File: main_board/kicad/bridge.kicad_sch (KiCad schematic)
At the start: 21 parts, among them Q1 IRFB3077, Q2 IRFB3077, Q3 IRFB3077, Q4 IRFB3077, Q5 IRFB3077, Q6 IRFB3077

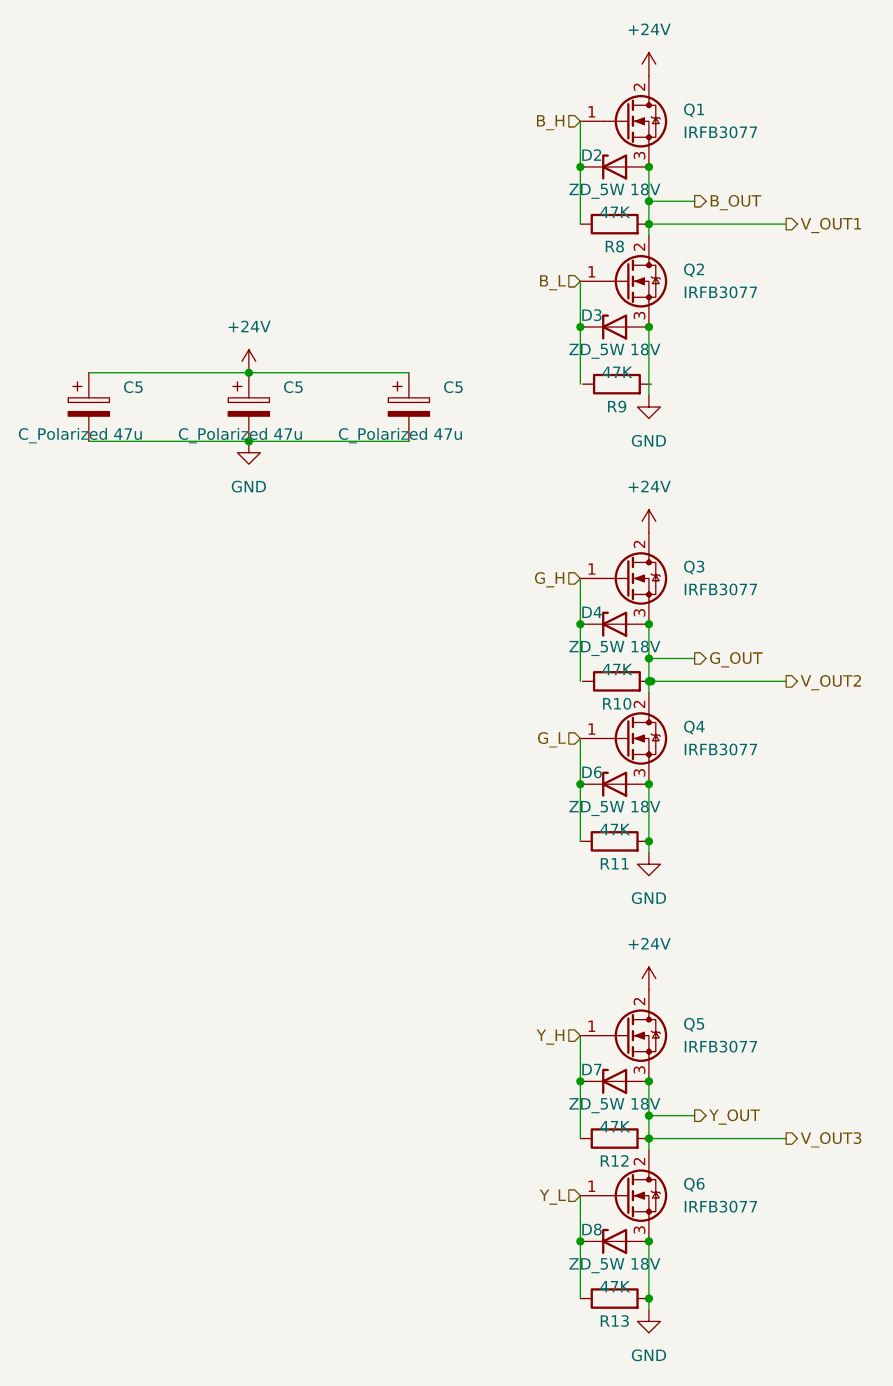
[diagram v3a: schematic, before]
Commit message: added LEDS and fuses
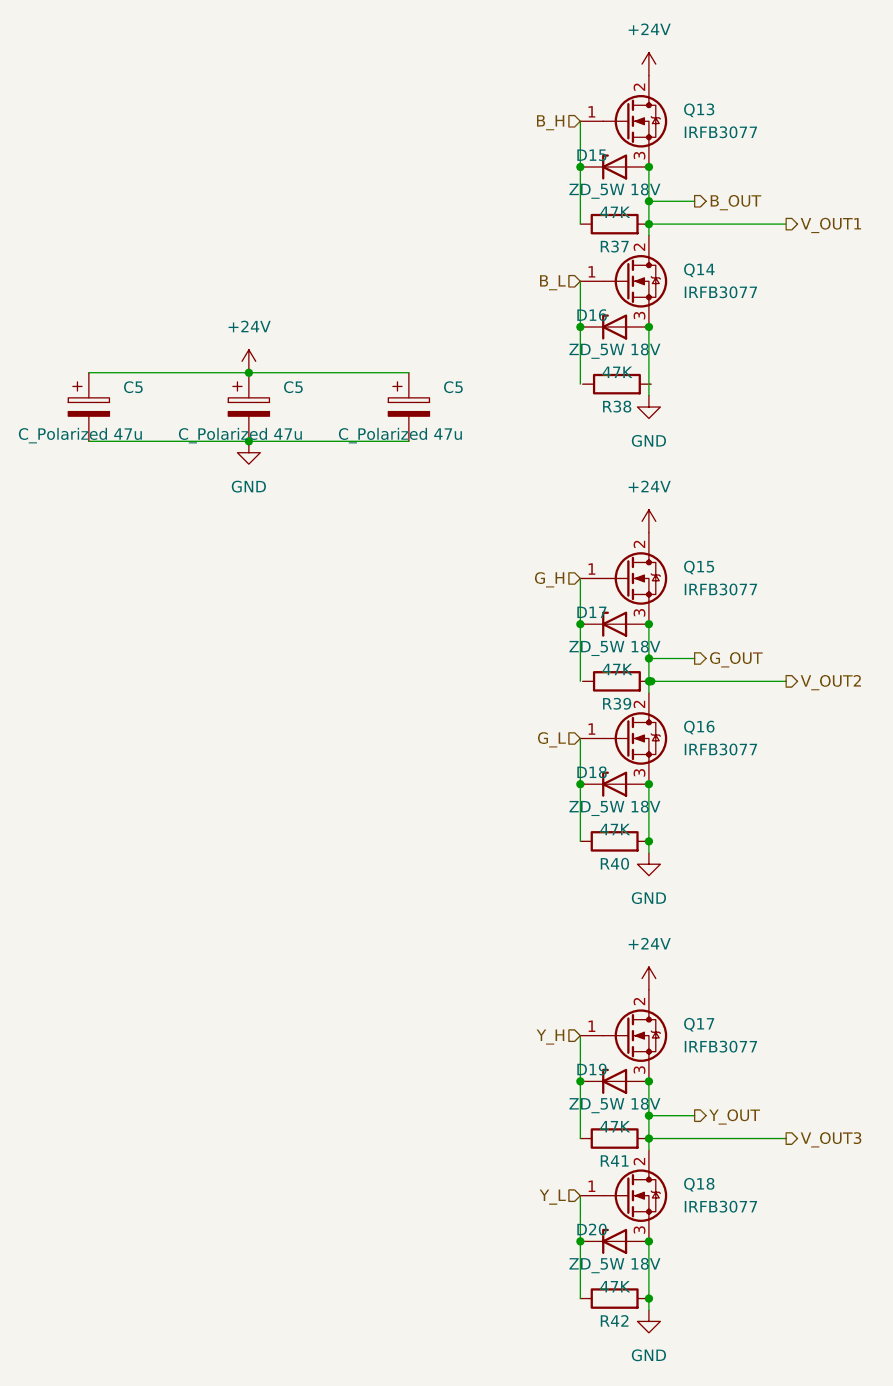
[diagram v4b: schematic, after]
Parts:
- renumbered D2 to D15, D3 to D16, D4 to D17, D6 to D18, D7 to D19, D8 to D20, Q1 to Q13, Q2 to Q14, Q3 to Q15, Q4 to Q16, Q5 to Q17, Q6 to Q18, R8 to R37, R9 to R38, R10 to R39, R11 to R40, R12 to R41, R13 to R42
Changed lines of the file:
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@@
   (symbol (lib_id "2022-lsd:IRFB3077") (at 114.3 137.16 0) (unit 1)
     (in_bom yes) (on_board yes) (dnp no) (fields_autoplaced)
-    (property "Reference" "Q5" (at 120.65 135.89 0)
+    (property "Reference" "Q17" (at 120.65 135.89 0)
       (effects (font (size 1.27 1.27)) (justify left))
     )
@@
   (symbol (lib_id "Device:R") (at 113.03 115.57 90) (unit 1)
     (in_bom yes) (on_board yes) (dnp no)
-    (property "Reference" "R11" (at 113.03 118.11 90)
+    (property "Reference" "R40" (at 113.03 118.11 90)
       (effects (font (size 1.27 1.27)))
     )
@@
   (symbol (lib_id "2022-lsd:IRFB3077") (at 114.3 86.36 0) (unit 1)
     (in_bom yes) (on_board yes) (dnp no)
-    (property "Reference" "Q3" (at 120.65 85.09 0)
+    (property "Reference" "Q15" (at 120.65 85.09 0)
       (effects (font (size 1.27 1.27)) (justify left))
     )
@@
   (symbol (lib_id "power:+24V") (at 116.84 81.28 0) (unit 1)
     (in_bom yes) (on_board yes) (dnp no) (fields_autoplaced)
-    (property "Reference" "#PWR026" (at 116.84 85.09 0)
+    (property "Reference" "#PWR069" (at 116.84 85.09 0)
       (effects (font (size 1.27 1.27)) hide)
     )
@@
   (symbol (lib_id "power:+24V") (at 72.39 63.5 0) (unit 1)
     (in_bom yes) (on_board yes) (dnp no) (fields_autoplaced)
-    (property "Reference" "#PWR021" (at 72.39 67.31 0)
+    (property "Reference" "#PWR065" (at 72.39 67.31 0)
       (effects (font (size 1.27 1.27)) hide)
     )
@@
   (symbol (lib_id "Diode:1N53xxB") (at 113.03 160.02 0) (unit 1)
     (in_bom yes) (on_board yes) (dnp no)
-    (property "Reference" "D8" (at 110.49 158.75 0)
+    (property "Reference" "D20" (at 110.49 158.75 0)
       (effects (font (size 1.27 1.27)))
     )
@@
   (symbol (lib_id "Device:R") (at 113.284 97.79 90) (unit 1)
     (in_bom yes) (on_board yes) (dnp no)
-    (property "Reference" "R10" (at 113.284 100.33 90)
+    (property "Reference" "R39" (at 113.284 100.33 90)
       (effects (font (size 1.27 1.27)))
     )
@@
   (symbol (lib_id "Diode:1N53xxB") (at 113.03 109.22 0) (unit 1)
     (in_bom yes) (on_board yes) (dnp no)
-    (property "Reference" "D6" (at 110.49 107.95 0)
+    (property "Reference" "D18" (at 110.49 107.95 0)
       (effects (font (size 1.27 1.27)))
     )
@@
   (symbol (lib_id "2022-lsd:IRFB3077") (at 114.3 154.94 0) (unit 1)
     (in_bom yes) (on_board yes) (dnp no) (fields_autoplaced)
-    (property "Reference" "Q6" (at 120.65 153.67 0)
+    (property "Reference" "Q18" (at 120.65 153.67 0)
       (effects (font (size 1.27 1.27)) (justify left))
     )
@@
   (symbol (lib_id "Diode:1N53xxB") (at 113.03 142.24 0) (unit 1)
     (in_bom yes) (on_board yes) (dnp no)
-    (property "Reference" "D7" (at 110.49 140.97 0)
+    (property "Reference" "D19" (at 110.49 140.97 0)
       (effects (font (size 1.27 1.27)))
     )
@@
   (symbol (lib_id "Device:R") (at 113.284 64.77 90) (unit 1)
     (in_bom yes) (on_board yes) (dnp no)
-    (property "Reference" "R9" (at 113.284 67.31 90)
+    (property "Reference" "R38" (at 113.284 67.31 90)
       (effects (font (size 1.27 1.27)))
     )
@@
   (symbol (lib_id "power:GND") (at 116.84 66.04 0) (unit 1)
     (in_bom yes) (on_board yes) (dnp no) (fields_autoplaced)
-    (property "Reference" "#PWR025" (at 116.84 72.39 0)
+    (property "Reference" "#PWR068" (at 116.84 72.39 0)
       (effects (font (size 1.27 1.27)) hide)
     )
@@
   (symbol (lib_id "power:+24V") (at 116.84 30.48 0) (unit 1)
     (in_bom yes) (on_board yes) (dnp no) (fields_autoplaced)
-    (property "Reference" "#PWR024" (at 116.84 34.29 0)
+    (property "Reference" "#PWR067" (at 116.84 34.29 0)
       (effects (font (size 1.27 1.27)) hide)
     )
@@
   (symbol (lib_id "Device:R") (at 113.03 46.99 90) (unit 1)
     (in_bom yes) (on_board yes) (dnp no)
-    (property "Reference" "R8" (at 113.03 49.53 90)
+    (property "Reference" "R37" (at 113.03 49.53 90)
       (effects (font (size 1.27 1.27)))
     )
@@
   (symbol (lib_id "power:GND") (at 72.39 71.12 0) (unit 1)
     (in_bom yes) (on_board yes) (dnp no) (fields_autoplaced)
-    (property "Reference" "#PWR023" (at 72.39 77.47 0)
+    (property "Reference" "#PWR066" (at 72.39 77.47 0)
       (effects (font (size 1.27 1.27)) hide)
     )
@@
   (symbol (lib_id "2022-lsd:IRFB3077") (at 114.3 53.34 0) (unit 1)
     (in_bom yes) (on_board yes) (dnp no) (fields_autoplaced)
-    (property "Reference" "Q2" (at 120.65 52.07 0)
+    (property "Reference" "Q14" (at 120.65 52.07 0)
       (effects (font (size 1.27 1.27)) (justify left))
     )
@@
   (symbol (lib_id "Diode:1N53xxB") (at 113.03 40.64 0) (unit 1)
     (in_bom yes) (on_board yes) (dnp no)
-    (property "Reference" "D2" (at 110.49 39.37 0)
+    (property "Reference" "D15" (at 110.49 39.37 0)
       (effects (font (size 1.27 1.27)))
     )
@@
   (symbol (lib_id "power:GND") (at 116.84 116.84 0) (unit 1)
     (in_bom yes) (on_board yes) (dnp no) (fields_autoplaced)
-    (property "Reference" "#PWR027" (at 116.84 123.19 0)
+    (property "Reference" "#PWR070" (at 116.84 123.19 0)
       (effects (font (size 1.27 1.27)) hide)
     )
@@
   (symbol (lib_id "power:+24V") (at 116.84 132.08 0) (unit 1)
     (in_bom yes) (on_board yes) (dnp no) (fields_autoplaced)
-    (property "Reference" "#PWR028" (at 116.84 135.89 0)
+    (property "Reference" "#PWR071" (at 116.84 135.89 0)
       (effects (font (size 1.27 1.27)) hide)
     )
@@
   (symbol (lib_id "power:GND") (at 116.84 167.64 0) (unit 1)
     (in_bom yes) (on_board yes) (dnp no) (fields_autoplaced)
-    (property "Reference" "#PWR029" (at 116.84 173.99 0)
+    (property "Reference" "#PWR072" (at 116.84 173.99 0)
       (effects (font (size 1.27 1.27)) hide)
     )
@@
   (symbol (lib_id "Device:R") (at 113.03 166.37 90) (unit 1)
     (in_bom yes) (on_board yes) (dnp no)
-    (property "Reference" "R13" (at 113.03 168.91 90)
+    (property "Reference" "R42" (at 113.03 168.91 90)
       (effects (font (size 1.27 1.27)))
     )
@@
   (symbol (lib_id "Device:R") (at 113.03 148.59 90) (unit 1)
     (in_bom yes) (on_board yes) (dnp no)
-    (property "Reference" "R12" (at 113.03 151.13 90)
+    (property "Reference" "R41" (at 113.03 151.13 90)
       (effects (font (size 1.27 1.27)))
     )
@@
   (symbol (lib_id "2022-lsd:IRFB3077") (at 114.3 104.14 0) (unit 1)
     (in_bom yes) (on_board yes) (dnp no)
-    (property "Reference" "Q4" (at 120.65 102.87 0)
+    (property "Reference" "Q16" (at 120.65 102.87 0)
       (effects (font (size 1.27 1.27)) (justify left))
     )
@@
   (symbol (lib_id "Diode:1N53xxB") (at 113.03 91.44 0) (unit 1)
     (in_bom yes) (on_board yes) (dnp no)
-    (property "Reference" "D4" (at 110.49 90.17 0)
+    (property "Reference" "D17" (at 110.49 90.17 0)
       (effects (font (size 1.27 1.27)))
     )
@@
   (symbol (lib_id "2022-lsd:IRFB3077") (at 114.3 35.56 0) (unit 1)
     (in_bom yes) (on_board yes) (dnp no) (fields_autoplaced)
-    (property "Reference" "Q1" (at 120.65 34.29 0)
+    (property "Reference" "Q13" (at 120.65 34.29 0)
       (effects (font (size 1.27 1.27)) (justify left))
     )
@@
   (symbol (lib_id "Diode:1N53xxB") (at 113.03 58.42 0) (unit 1)
     (in_bom yes) (on_board yes) (dnp no)
-    (property "Reference" "D3" (at 110.49 57.15 0)
-      (effects (font (size 1.27 1.27)))
-    )
+    (property "Reference" "D16" (at 110.49 57.15 0)
+      (effects (font (size 1.27 1.27)))
+    )

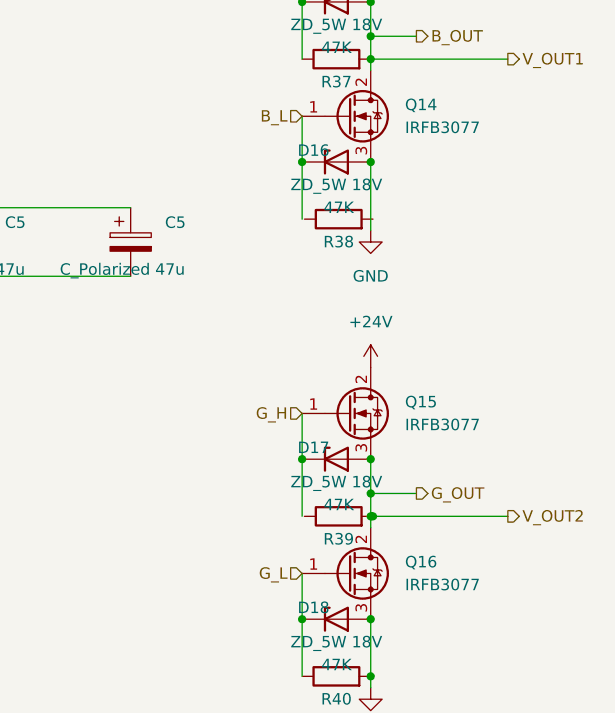
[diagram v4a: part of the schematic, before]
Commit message: resolved ERC
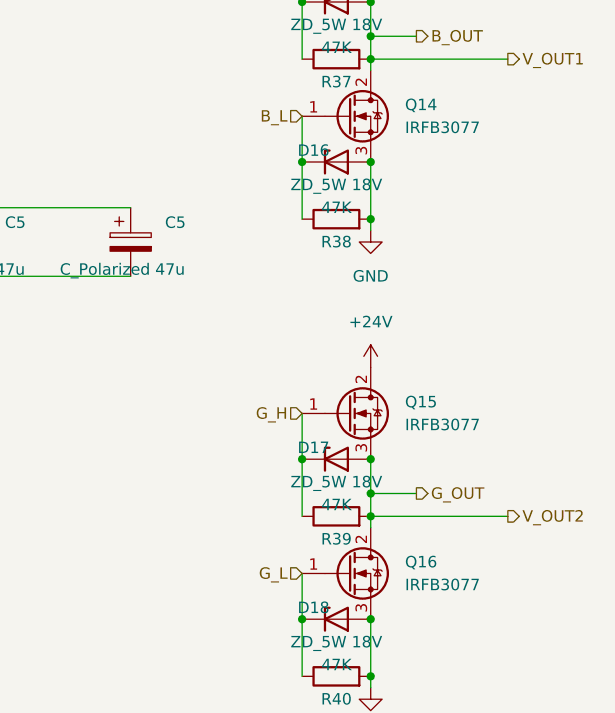
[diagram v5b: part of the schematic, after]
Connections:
- net B_L: now also R38.1
- net GND: now also R38.2
- net G_H: now also R39.1
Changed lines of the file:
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@@
   (junction (at 109.22 160.02) (diameter 0) (color 0 0 0 0)
   )
+  (junction (at 109.22 91.44) (diameter 0) (color 0 0 0 0)
+  )
   (junction (at 116.84 40.64) (diameter 0) (color 0 0 0 0)
   )
   (junction (at 116.84 146.05) (diameter 0) (color 0 0 0 0)
   )
+  (junction (at 116.84 64.77) (diameter 0) (color 0 0 0 0)
+  )
   (junction (at 109.22 142.24) (diameter 0) (color 0 0 0 0)
   )
@@
   (junction (at 116.84 109.22) (diameter 0) (color 0 0 0 0)
   )
-  (junction (at 109.22 91.44) (diameter 0) (color 0 0 0 0)
-  )
   (junction (at 116.84 46.99) (diameter 0) (color 0 0 0 0)
   )
-  (junction (at 117.094 97.79) (diameter 0) (color 0 0 0 0)
-  )
   (junction (at 116.84 91.44) (diameter 0) (color 0 0 0 0)
   )
@@
     (stroke (width 0) (type default))
   )
-  (wire (pts (xy 116.84 58.42) (xy 116.84 66.04))
+  (wire (pts (xy 116.84 58.42) (xy 116.84 64.77))
     (stroke (width 0) (type default))
   )
@@
     (stroke (width 0) (type default))
   )
-  (wire (pts (xy 116.84 97.79) (xy 117.094 97.79))
+  (wire (pts (xy 116.84 97.79) (xy 132.08 97.79))
     (stroke (width 0) (type default))
   )
@@
     (stroke (width 0) (type default))
   )
+  (wire (pts (xy 116.84 64.77) (xy 116.84 66.04))
+    (stroke (width 0) (type default))
+  )
   (wire (pts (xy 116.84 148.59) (xy 132.08 148.59))
     (stroke (width 0) (type default))
@@
     (stroke (width 0) (type default))
   )
+  (wire (pts (xy 109.22 91.44) (xy 109.22 97.79))
+    (stroke (width 0) (type default))
+  )
   (wire (pts (xy 116.84 91.44) (xy 116.84 95.25))
     (stroke (width 0) (type default))
@@
   )
   (wire (pts (xy 109.22 58.42) (xy 109.22 64.77))
-    (stroke (width 0) (type default))
-  )
-  (wire (pts (xy 109.22 91.44) (xy 109.22 97.79))
-    (stroke (width 0) (type default))
-  )
-  (wire (pts (xy 117.094 97.79) (xy 132.08 97.79))
     (stroke (width 0) (type default))
   )
@@
     )
   )
-  (symbol (lib_id "Device:R") (at 113.284 97.79 90) (unit 1)
-    (in_bom yes) (on_board yes) (dnp no)
-    (property "Reference" "R39" (at 113.284 100.33 90)
-      (effects (font (size 1.27 1.27)))
-    )
-    (property "Value" "47K" (at 113.284 96.52 90)
-      (effects (font (size 1.27 1.27)))
-    )
-    (property "Footprint" "" (at 113.284 99.568 90)
-      (effects (font (size 1.27 1.27)) hide)
-    )
-    (property "Datasheet" "~" (at 113.284 97.79 0)
+  (symbol (lib_id "Device:R") (at 113.03 97.79 90) (unit 1)
+    (in_bom yes) (on_board yes) (dnp no)
+    (property "Reference" "R39" (at 113.03 100.33 90)
+      (effects (font (size 1.27 1.27)))
+    )
+    (property "Value" "47K" (at 113.03 96.52 90)
+      (effects (font (size 1.27 1.27)))
+    )
+    (property "Footprint" "" (at 113.03 99.568 90)
+      (effects (font (size 1.27 1.27)) hide)
+    )
+    (property "Datasheet" "~" (at 113.03 97.79 0)
       (effects (font (size 1.27 1.27)) hide)
     )
@@
     )
   )
-  (symbol (lib_id "Device:R") (at 113.284 64.77 90) (unit 1)
-    (in_bom yes) (on_board yes) (dnp no)
-    (property "Reference" "R38" (at 113.284 67.31 90)
-      (effects (font (size 1.27 1.27)))
-    )
-    (property "Value" "47K" (at 113.284 63.5 90)
-      (effects (font (size 1.27 1.27)))
-    )
-    (property "Footprint" "" (at 113.284 66.548 90)
-      (effects (font (size 1.27 1.27)) hide)
-    )
-    (property "Datasheet" "~" (at 113.284 64.77 0)
-      (effects (font (size 1.27 1.27)) hide)
-    )
+  (symbol (lib_id "Device:R") (at 113.03 64.77 90) (unit 1)
+    (in_bom yes) (on_board yes) (dnp no)
+    (property "Reference" "R38" (at 113.03 67.31 90)
+      (effects (font (size 1.27 1.27)))
+    )
+    (property "Value" "47K" (at 113.03 63.5 90)
+      (effects (font (size 1.27 1.27)))
+    )
+    (property "Footprint" "" (at 113.03 66.548 90)
+      (effects (font (size 1.27 1.27)) hide)
+    )
+    (property "Datasheet" "~" (at 113.03 64.77 0)
+      (effects (font (size 1.27 1.27)) hide)
+    )

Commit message: added footprints
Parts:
- C5: footprint (none) -> Capacitor_THT:CP_Radial_D8.0mm_P3.50mm
- R37, R38, R39, R40, R41, R42: footprint (none) -> Resistor_THT:R_Axial_DIN0207_L6.3mm_D2.5mm_P7.62mm_Horizontal
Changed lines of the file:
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@@
       (effects (font (size 1.27 1.27)) (justify left))
     )
-    (property "Footprint" "" (at 73.3552 71.12 0)
+    (property "Footprint" "Capacitor_THT:CP_Radial_D8.0mm_P3.50mm" (at 73.3552 71.12 0)
       (effects (font (size 1.27 1.27)) hide)
     )
@@
       (effects (font (size 1.27 1.27)))
     )
-    (property "Footprint" "" (at 113.03 117.348 90)
+    (property "Footprint" "Resistor_THT:R_Axial_DIN0207_L6.3mm_D2.5mm_P7.62mm_Horizontal" (at 113.03 117.348 90)
       (effects (font (size 1.27 1.27)) hide)
     )
@@
       (effects (font (size 1.27 1.27)))
     )
-    (property "Footprint" "" (at 113.03 99.568 90)
+    (property "Footprint" "Resistor_THT:R_Axial_DIN0207_L6.3mm_D2.5mm_P7.62mm_Horizontal" (at 113.03 99.568 90)
       (effects (font (size 1.27 1.27)) hide)
     )
@@
       (effects (font (size 1.27 1.27)))
     )
-    (property "Footprint" "" (at 113.03 66.548 90)
+    (property "Footprint" "Resistor_THT:R_Axial_DIN0207_L6.3mm_D2.5mm_P7.62mm_Horizontal" (at 113.03 66.548 90)
       (effects (font (size 1.27 1.27)) hide)
     )
@@
       (effects (font (size 1.27 1.27)))
     )
-    (property "Footprint" "" (at 113.03 48.768 90)
+    (property "Footprint" "Resistor_THT:R_Axial_DIN0207_L6.3mm_D2.5mm_P7.62mm_Horizontal" (at 113.03 48.768 90)
       (effects (font (size 1.27 1.27)) hide)
     )
@@
       (effects (font (size 1.27 1.27)) (justify left))
     )
-    (property "Footprint" "" (at 91.1352 71.12 0)
+    (property "Footprint" "Capacitor_THT:CP_Radial_D8.0mm_P3.50mm" (at 91.1352 71.12 0)
       (effects (font (size 1.27 1.27)) hide)
     )
@@
       (effects (font (size 1.27 1.27)))
     )
-    (property "Footprint" "" (at 113.03 168.148 90)
+    (property "Footprint" "Resistor_THT:R_Axial_DIN0207_L6.3mm_D2.5mm_P7.62mm_Horizontal" (at 113.03 168.148 90)
       (effects (font (size 1.27 1.27)) hide)
     )
@@
       (effects (font (size 1.27 1.27)))
     )
-    (property "Footprint" "" (at 113.03 150.368 90)
+    (property "Footprint" "Resistor_THT:R_Axial_DIN0207_L6.3mm_D2.5mm_P7.62mm_Horizontal" (at 113.03 150.368 90)
       (effects (font (size 1.27 1.27)) hide)
     )
@@
       (effects (font (size 1.27 1.27)) (justify left))
     )
-    (property "Footprint" "" (at 55.5752 71.12 0)
-      (effects (font (size 1.27 1.27)) hide)
-    )
+    (property "Footprint" "Capacitor_THT:CP_Radial_D8.0mm_P3.50mm" (at 55.5752 71.12 0)
+      (effects (font (size 1.27 1.27)) hide)
+    )
